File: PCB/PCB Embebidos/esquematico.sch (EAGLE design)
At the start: 30 parts, among them IC1 LM358N, IC2 317T, T1 BT138-V

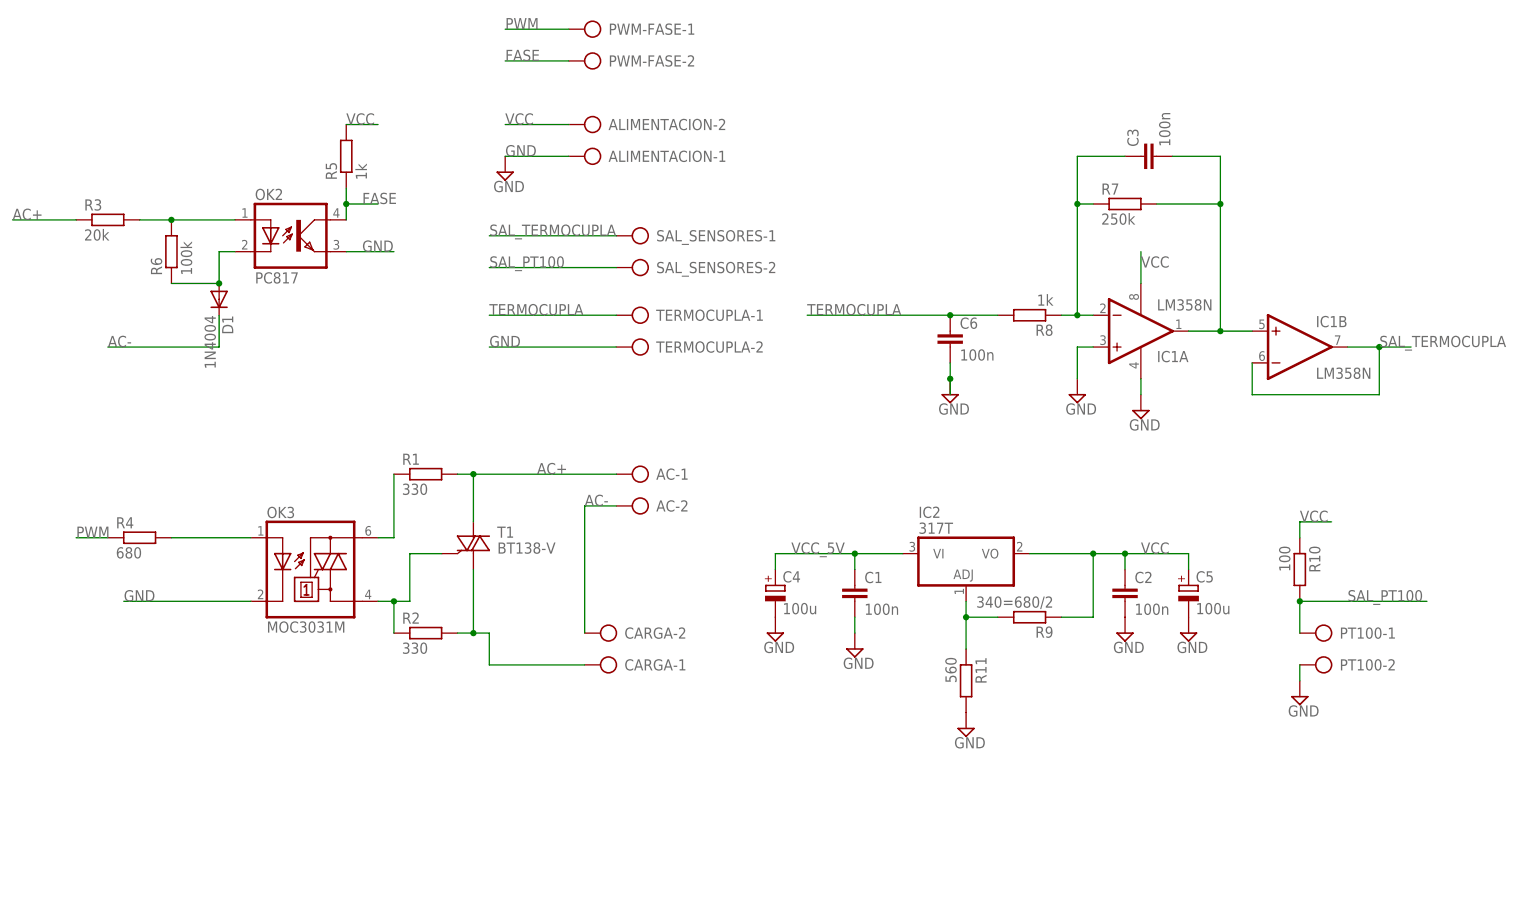
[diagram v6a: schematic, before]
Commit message: Borre lo del PT100 y agrege las cosas para hacer el control del cooler. Falta ordenar un poco, ver si se puede achicar mas, y volver a rutear
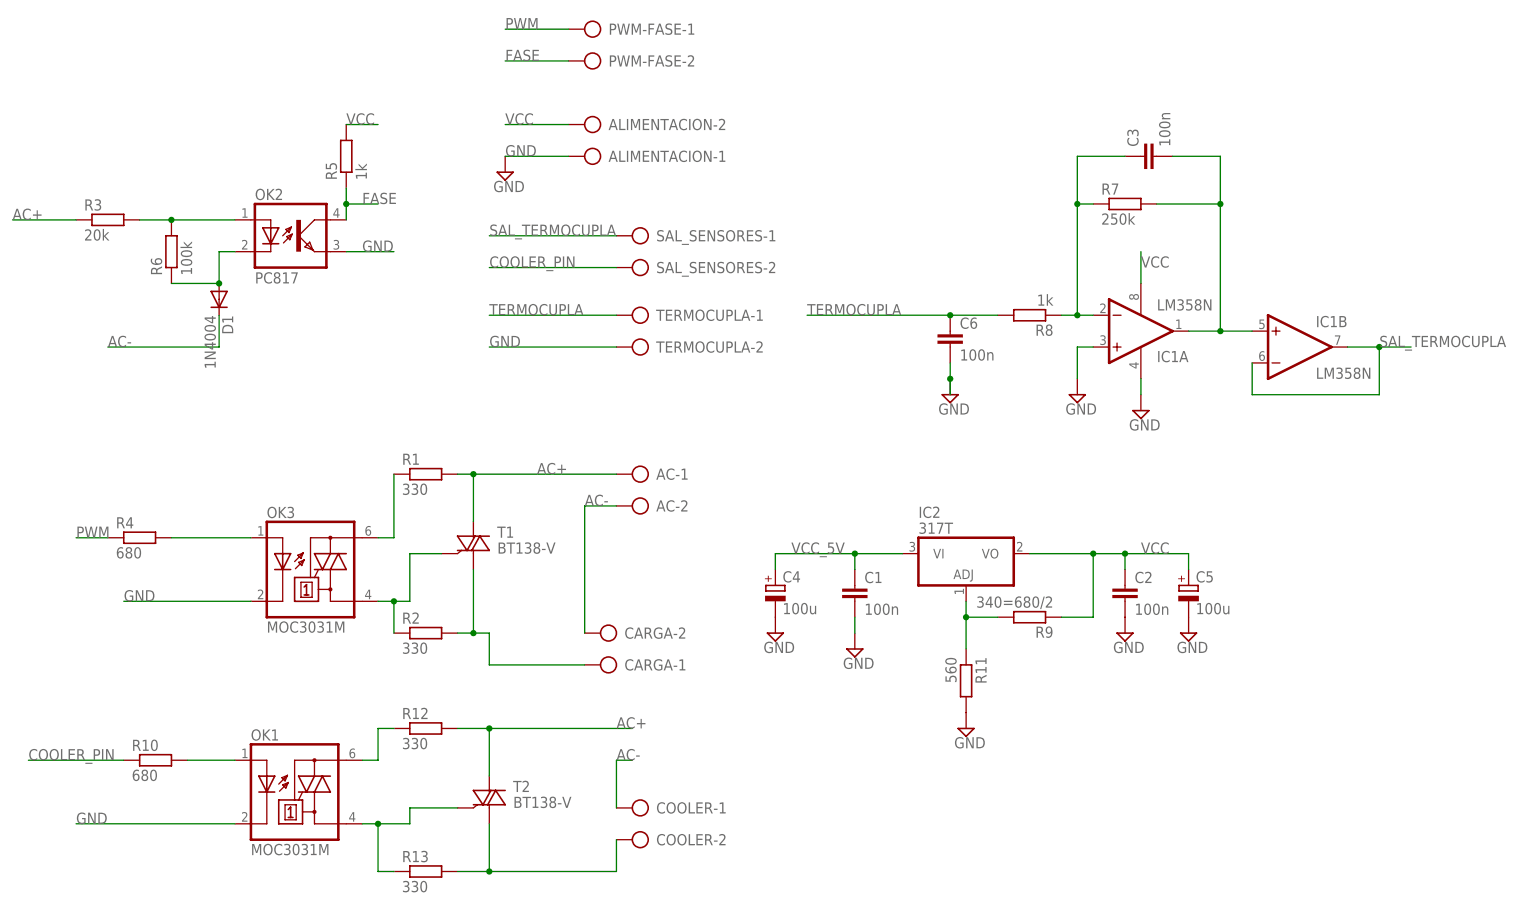
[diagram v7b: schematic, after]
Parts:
- removed PT100: (no value), con-ptr500:AK300/2
- added COOLER: (no value), con-ptr500:AK300/2
- added OK1: MOC3031M, optocoupler:MOC3031M
- added R12, R13: 330, resistor:R-EU_R1206
- added T2: BT138-V, triac:BT138-V
- R10: value 100 -> 680
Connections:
- removed net SAL_PT100: PT100-1.KL, R10.2, SAL_SENSORES-2.KL
- new net COOLER_PIN: R10.1, SAL_SENSORES-2.KL
- new net N$11: OK1.A, R10.2
- new net N$12: OK1.A2, R12.1
- new net N$15: OK1.A1, R13.1, T2.G
- new net N$17: COOLER-2.KL, R13.2, T2.A1
- net AC+: now also R12.2, T2.A2
- net AC-: now also COOLER-1.KL
- net GND: now also OK1.C; no longer PT100-2.KL
- net VCC: no longer R10.1
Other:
- moved on the sheet: R10

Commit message: Tuve que rehacer la placa porque habian quedado muy finas las pistas. El codigo no lo modifique, y parece estar andando todo bien. Mañana le voy a poner disipadores a los triacs y voy a empezar a poner las curvas de referencia
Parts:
- R1, R12, R13, R2: value 330 -> 560
- R3: value 20k -> 100k
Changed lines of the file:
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@@
 </variantdefs>
 <classes>
-<class number="0" name="default" width="0" drill="0">
+<class number="0" name="default" width="0.9906" drill="0.9906">
+<clearance class="0" value="0.762"/>
 </class>
 </classes>
 <parts>
 <part name="T1" library="triac" deviceset="BT138" device="-V"/>
-<part name="R1" library="resistor" deviceset="R-EU_" device="R1206" value="330"/>
-<part name="R2" library="resistor" deviceset="R-EU_" device="R1206" value="330"/>
+<part name="R1" library="resistor" deviceset="R-EU_" device="R1206" value="560"/>
+<part name="R2" library="resistor" deviceset="R-EU_" device="R1206" value="560"/>
 <part name="R4" library="resistor" deviceset="R-EU_" device="R1206" value="680"/>
 <part name="SUPPLY1" library="supply2" deviceset="GND" device=""/>
@@
 <part name="OK3" library="optocoupler" deviceset="MOC30*" device="" technology="31M"/>
 <part name="D1" library="diode" deviceset="1N4004" device=""/>
-<part name="R3" library="resistor" deviceset="R-EU_" device="0207/10" value="20k"/>
+<part name="R3" library="resistor" deviceset="R-EU_" device="0207/10" value="100k"/>
 <part name="R5" library="resistor" deviceset="R-EU_" device="R1206" value="1k"/>
 <part name="R6" library="resistor" deviceset="R-EU_" device="R1206" value="100k"/>
@@
 <part name="OK1" library="optocoupler" deviceset="MOC30*" device="" technology="31M"/>
 <part name="R10" library="resistor" deviceset="R-EU_" device="R1206" value="680"/>
-<part name="R12" library="resistor" deviceset="R-EU_" device="R1206" value="330"/>
-<part name="R13" library="resistor" deviceset="R-EU_" device="R1206" value="330"/>
+<part name="R12" library="resistor" deviceset="R-EU_" device="R1206" value="560"/>
+<part name="R13" library="resistor" deviceset="R-EU_" device="R1206" value="560"/>
 <part name="T2" library="triac" deviceset="BT138" device="-V"/>
 <part name="COOLER" library="con-ptr500" deviceset="AK300/2" device=""/>
